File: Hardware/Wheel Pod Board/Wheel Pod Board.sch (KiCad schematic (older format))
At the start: 30 parts, among them J1 Conn_RJ-45, P1 UIM240XX_Stepper_Conn, P2 RS232, P3 ST_SWD_Connector, P4 SyRen, P5 BATT, U1 STM32F401RCT6, U2 SN75176BDR, U3 ZXCT1107, U4 ZXCT1107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

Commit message: Add ADC channels to cube, kicad something
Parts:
- P4: footprint MAVRIC_footprints:1x3_SMD_header -> Wire_Pads:SolderWirePad_3x_0-8mmDrill
- P5: footprint MAVRIC_footprints:1x2_SMD_header -> Wire_Pads:SolderWirePad_2x_0-8mmDrill
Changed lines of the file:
@@
 $EndComp
 $Comp
-L GND #PWR09
+L GND #PWR08
 U 1 1 54F82F5F
 P 7300 5750
-F 0 "#PWR09" H 7300 5500 60  0001 C CNN
+F 0 "#PWR08" H 7300 5500 60  0001 C CNN
 F 1 "GND" H 7300 5600 60  0000 C CNN
 F 2 "" H 7300 5750 60  0000 C CNN
@@
 $EndComp
 $Comp
-L GND #PWR010
+L GND #PWR09
 U 1 1 54F83FA9
 P 6550 5050
-F 0 "#PWR010" H 6550 4800 60  0001 C CNN
+F 0 "#PWR09" H 6550 4800 60  0001 C CNN
 F 1 "GND" H 6550 4900 60  0000 C CNN
 F 2 "" H 6550 5050 60  0000 C CNN
@@
 Connection ~ 7250 3900
 $Comp
-L +3V3 #PWR011
+L +3V3 #PWR010
 U 1 1 54F898ED
 P 4350 7400
-F 0 "#PWR011" H 4350 7250 60  0001 C CNN
+F 0 "#PWR010" H 4350 7250 60  0001 C CNN
 F 1 "+3V3" H 4350 7540 60  0000 C CNN
 F 2 "" H 4350 7400 60  0000 C CNN
@@
 	4350 7300 5000 7300
 $Comp
-L PWR_FLAG #FLG012
+L PWR_FLAG #FLG011
 U 1 1 54F89ADE
 P 4650 7350
-F 0 "#FLG012" H 4650 7445 30  0001 C CNN
+F 0 "#FLG011" H 4650 7445 30  0001 C CNN
 F 1 "PWR_FLAG" H 4650 7530 30  0000 C CNN
 F 2 "" H 4650 7350 60  0000 C CNN
@@
 $EndComp
 $Comp
-L +5V #PWR013
+L +5V #PWR012
 U 1 1 54F89B19
 P 4400 6800
-F 0 "#PWR013" H 4400 6650 60  0001 C CNN
+F 0 "#PWR012" H 4400 6650 60  0001 C CNN
 F 1 "+5V" H 4400 6940 60  0000 C CNN
 F 2 "" H 4400 6800 60  0000 C CNN
@@
 $EndComp
 $Comp
-L GND #PWR014
+L GND #PWR013
 U 1 1 54F91E0A
 P 10800 2450
-F 0 "#PWR014" H 10800 2200 60  0001 C CNN
+F 0 "#PWR013" H 10800 2200 60  0001 C CNN
 F 1 "GND" H 10800 2300 60  0000 C CNN
 F 2 "" H 10800 2450 60  0000 C CNN
@@
 F 0 "P5" H 6700 3700 50  0000 C CNN
 F 1 "BATT" H 6700 3400 50  0000 C CNN
-F 2 "MAVRIC_footprints:1x2_SMD_header" H 6700 3550 60  0001 C CNN
+F 2 "Wire_Pads:SolderWirePad_2x_0-8mmDrill" H 6700 3550 60  0001 C CNN
 F 3 "" H 6700 3550 60  0000 C CNN
 	1    6700 3550
@@
 $EndComp
 $Comp
-L GND #PWR015
+L GND #PWR014
 U 1 1 54F97284
 P 8450 5050
-F 0 "#PWR015" H 8450 4800 60  0001 C CNN
+F 0 "#PWR014" H 8450 4800 60  0001 C CNN
 F 1 "GND" H 8450 4900 60  0000 C CNN
 F 2 "" H 8450 5050 60  0000 C CNN
@@
 	10950 3500 10950 3800
 $Comp
-L GND #PWR016
+L GND #PWR015
 U 1 1 54F987F3
 P 10950 3800
-F 0 "#PWR016" H 10950 3550 60  0001 C CNN
+F 0 "#PWR015" H 10950 3550 60  0001 C CNN
 F 1 "GND" H 10950 3650 60  0000 C CNN
 F 2 "" H 10950 3800 60  0000 C CNN
@@
 Connection ~ 9150 3600
 $Comp
-L +12V #PWR017
+L +12V #PWR016
 U 1 1 54F9E120
 P 10700 3800
-F 0 "#PWR017" H 10700 3650 60  0001 C CNN
+F 0 "#PWR016" H 10700 3650 60  0001 C CNN
 F 1 "+12V" H 10700 3940 60  0000 C CNN
 F 2 "" H 10700 3800 60  0000 C CNN
@@
 $EndComp
 $Comp
-L PWR_FLAG #FLG018
+L PWR_FLAG #FLG017
 U 1 1 54F9E134
 P 7050 3600
-F 0 "#FLG018" H 7050 3695 30  0001 C CNN
+F 0 "#FLG017" H 7050 3695 30  0001 C CNN
 F 1 "PWR_FLAG" H 7050 3780 30  0000 C CNN
 F 2 "" H 7050 3600 60  0000 C CNN
@@
 $EndComp
 $Comp
-L PWR_FLAG #FLG019
+L PWR_FLAG #FLG018
 U 1 1 54F9E417
 P 7050 3500
-F 0 "#FLG019" H 7050 3595 30  0001 C CNN
+F 0 "#FLG018" H 7050 3595 30  0001 C CNN
 F 1 "PWR_FLAG" H 7050 3680 30  0000 C CNN
 F 2 "" H 7050 3500 60  0000 C CNN
@@
 Connection ~ 9750 3500
 $Comp
-L +3V3 #PWR020
+L +3V3 #PWR019
 U 1 1 54FA32A7
 P 7350 1500
-F 0 "#PWR020" H 7350 1350 60  0001 C CNN
+F 0 "#PWR019" H 7350 1350 60  0001 C CNN
 F 1 "+3V3" H 7350 1640 60  0000 C CNN
 F 2 "" H 7350 1500 60  0000 C CNN
@@
 $EndComp
 $Comp
-L +5V #PWR021
+L +5V #PWR020
 U 1 1 54FA4C38
 P 3450 6750
-F 0 "#PWR021" H 3450 6600 60  0001 C CNN
+F 0 "#PWR020" H 3450 6600 60  0001 C CNN
 F 1 "+5V" H 3450 6890 60  0000 C CNN
 F 2 "" H 3450 6750 60  0000 C CNN
@@
 Stp+12V
 $Comp
-L +5V #PWR022
+L +5V #PWR021
 U 1 1 54FACDEA
 P 7600 5850
-F 0 "#PWR022" H 7600 5700 60  0001 C CNN
+F 0 "#PWR021" H 7600 5700 60  0001 C CNN
 F 1 "+5V" H 7600 5990 60  0000 C CNN
 F 2 "" H 7600 5850 60  0000 C CNN
@@
 	10450 6050 10450 6100
 $Comp
-L GND #PWR023
+L GND #PWR022
 U 1 1 54FB0646
 P 10450 6100
-F 0 "#PWR023" H 10450 5850 60  0001 C CNN
+F 0 "#PWR022" H 10450 5850 60  0001 C CNN
 F 1 "GND" H 10450 5950 60  0000 C CNN
 F 2 "" H 10450 6100 60  0000 C CNN
@@
 	4400 6900 5000 6900
 $Comp
-L PWR_FLAG #FLG024
+L PWR_FLAG #FLG023
 U 1 1 54F9E182
 P 4650 6850
-F 0 "#FLG024" H 4650 6945 30  0001 C CNN
+F 0 "#FLG023" H 4650 6945 30  0001 C CNN
 F 1 "PWR_FLAG" H 4650 7030 30  0000 C CNN
 F 2 "" H 4650 6850 60  0000 C CNN
@@
 Connection ~ 4850 7400
 $Comp
-L GND #PWR025
+L GND #PWR024
 U 1 1 54F9E9CC
 P 4850 7500
-F 0 "#PWR025" H 4850 7250 60  0001 C CNN
+F 0 "#PWR024" H 4850 7250 60  0001 C CNN
 F 1 "GND" H 4850 7350 60  0000 C CNN
 F 2 "" H 4850 7500 60  0000 C CNN
@@
 F 0 "P4" H 10150 4050 50  0000 C CNN
 F 1 "SyRen" H 10150 3650 50  0000 C CNN
-F 2 "MAVRIC_footprints:1x3_SMD_header" H 10150 3850 60  0001 C CNN
+F 2 "Wire_Pads:SolderWirePad_3x_0-8mmDrill" H 10150 3850 60  0001 C CNN
 F 3 "" H 10150 3850 60  0000 C CNN
 	1    10150 3850

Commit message: Progress on new pcb route
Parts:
- P3: footprint MAVRIC_footprints:1x6_SMD_header -> MAVRIC_footprints:SolderWirePad_6xInline_0-8mmDrill
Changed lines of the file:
@@
 F 0 "P3" H 9200 6300 50  0000 C CNN
 F 1 "ST_SWD_Connector" H 9200 5600 50  0000 C CNN
-F 2 "MAVRIC_footprints:1x6_SMD_header" H 9200 5950 60  0001 C CNN
+F 2 "MAVRIC_footprints:SolderWirePad_6xInline_0-8mmDrill" H 9200 5950 60  0001 C CNN
 F 3 "" H 9200 5950 60  0000 C CNN
 	1    9200 5950

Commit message: Attach 485 TX enable to micro
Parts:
- P3: footprint MAVRIC_footprints:SolderWirePad_6xInline_0-8mmDrill -> MAVRIC_footprints:1x6_SMD_header
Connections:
- net TX_EN: now reaches U1.50 (PA15)
- net TX_EN: now also U2.2 (~RE), U2.3 (DE)
- no-connect marks 41 -> 40
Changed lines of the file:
@@
 F 0 "P3" H 9200 6300 50  0000 C CNN
 F 1 "ST_SWD_Connector" H 9200 5600 50  0000 C CNN
-F 2 "MAVRIC_footprints:SolderWirePad_6xInline_0-8mmDrill" H 9200 5950 60  0001 C CNN
+F 2 "MAVRIC_footprints:1x6_SMD_header" H 9200 5950 60  0001 C CNN
 F 3 "" H 9200 5950 60  0000 C CNN
 	1    9200 5950
@@
 NoConn ~ 1650 2250
 NoConn ~ 1650 2350
-NoConn ~ 1650 2650
 NoConn ~ 1650 3000
 NoConn ~ 1650 3100
@@
 Text Label 7600 5650 2    60   ~ 0
 Stp+12V
+Wire Wire Line
+	1650 2650 1800 2650
+Text Label 1800 2650 0    60   ~ 0
+TX_EN
+Text Label 1750 7000 2    60   ~ 0
+TX_EN
 $EndSCHEMATC

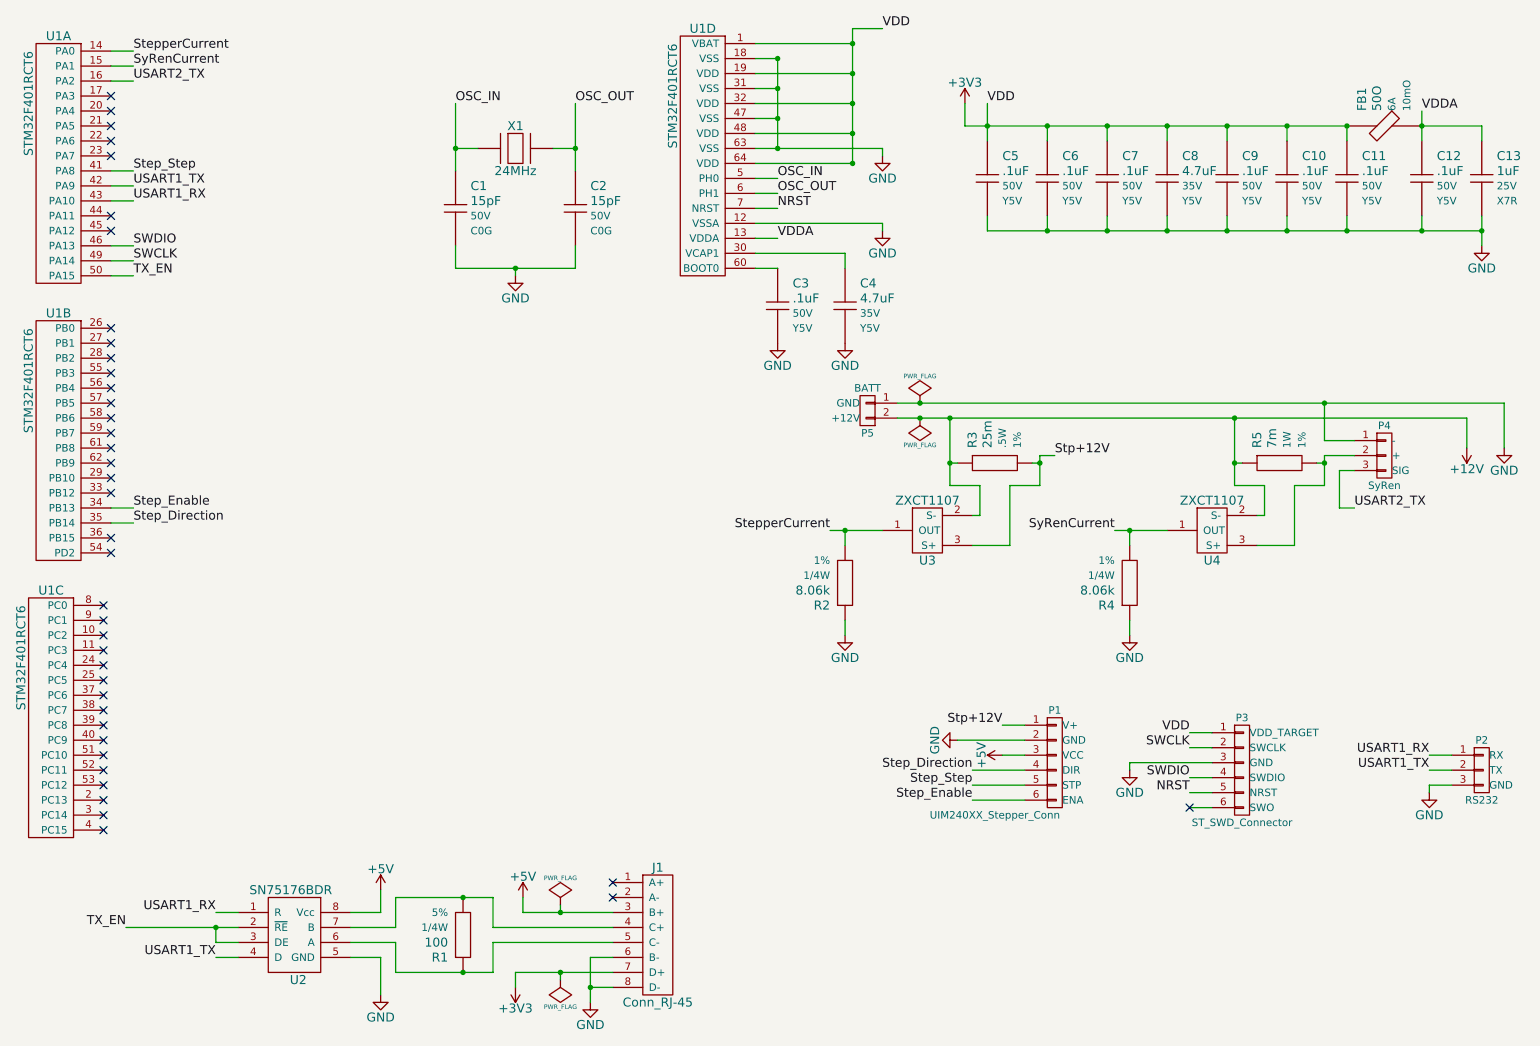
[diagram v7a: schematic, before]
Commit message: Add red and green LEDs to board
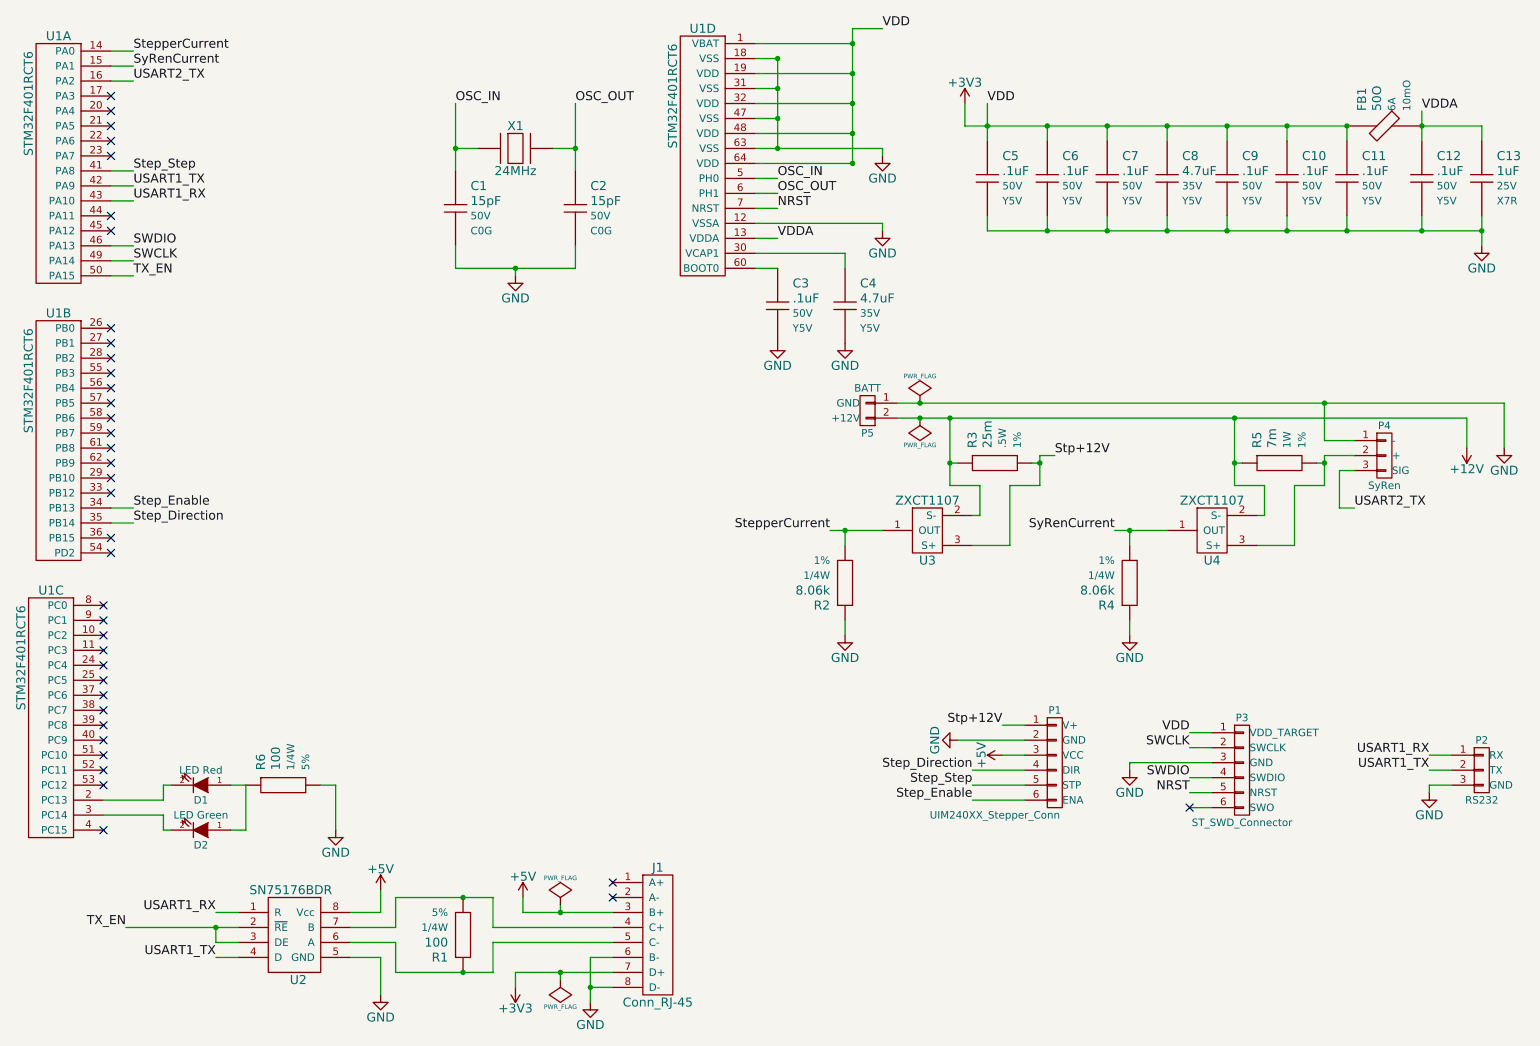
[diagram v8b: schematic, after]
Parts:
- added D1: LED Red, Resistors_SMD:R_0805_HandSoldering, symbol LED
- added D2: LED Green, Resistors_SMD:R_0805_HandSoldering, symbol LED
- added R6: 100, Resistors_SMD:R_1206_HandSoldering, symbol Resistor
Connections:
- net GND: now also R6.2
- net at U1.2 (PC13): now also D1.2 (K)
- net at U1.3 (PC14): now also D2.2 (K)
- new net: D1.1 (A), D2.1 (A), R6.1
- no-connect marks 40 -> 38
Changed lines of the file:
@@
 LIBS:MAVRIClib
 LIBS:Connectors
+LIBS:Actives
 LIBS:Wheel Pod Board-cache
 EELAYER 25 0
@@
 Connection ~ 6100 1400
 Wire Wire Line
-	5950 1800 6800 1800
+	5950 1800 6100 1800
+Wire Wire Line
+	6100 1800 6800 1800
 Connection ~ 6100 1800
 Wire Wire Line
@@
 Connection ~ 6600 1100
 Wire Wire Line
-	6100 1200 6100 1800
-Wire Wire Line
-	6600 1000 6600 1900
+	6100 1200 6100 1400
+Wire Wire Line
+	6100 1400 6100 1600
+Wire Wire Line
+	6100 1600 6100 1800
+Wire Wire Line
+	6600 1000 6600 1100
+Wire Wire Line
+	6600 1100 6600 1300
+Wire Wire Line
+	6600 1300 6600 1500
+Wire Wire Line
+	6600 1500 6600 1700
+Wire Wire Line
+	6600 1700 6600 1900
 Wire Wire Line
 	5950 2600 6100 2600
@@
 	2350 7100 2500 7100
 Wire Wire Line
-	1750 7000 2500 7000
+	1750 7000 2350 7000
+Wire Wire Line
+	2350 7000 2500 7000
 Wire Wire Line
 	2500 7200 2350 7200
@@
 	9900 1650 9900 1750
 Wire Wire Line
-	7500 1500 7500 1750
+	7500 1500 7500 1650
+Wire Wire Line
+	7500 1650 7500 1750
 Connection ~ 7500 1650
 Wire Wire Line
@@
 Connection ~ 9900 2350
 Wire Wire Line
-	10400 1550 10400 1750
+	10400 1550 10400 1650
+Wire Wire Line
+	10400 1650 10400 1750
 Connection ~ 9900 1650
 Connection ~ 10400 1650
@@
 	10800 1650 10800 1750
 Wire Wire Line
-	10800 2250 10800 2450
+	10800 2250 10800 2350
+Wire Wire Line
+	10800 2350 10800 2450
 Wire Wire Line
 	10400 2350 10400 2250
@@
 	10400 1650 10800 1650
 Wire Wire Line
-	7500 2350 10800 2350
-Wire Wire Line
-	7350 1650 9900 1650
+	7500 2350 7900 2350
+Wire Wire Line
+	7900 2350 8300 2350
+Wire Wire Line
+	8300 2350 8700 2350
+Wire Wire Line
+	8700 2350 9100 2350
+Wire Wire Line
+	9100 2350 9500 2350
+Wire Wire Line
+	9500 2350 9900 2350
+Wire Wire Line
+	9900 2350 10400 2350
+Wire Wire Line
+	10400 2350 10800 2350
+Wire Wire Line
+	7350 1650 7500 1650
+Wire Wire Line
+	7500 1650 7900 1650
+Wire Wire Line
+	7900 1650 8300 1650
+Wire Wire Line
+	8300 1650 8700 1650
+Wire Wire Line
+	8700 1650 9100 1650
+Wire Wire Line
+	9100 1650 9500 1650
+Wire Wire Line
+	9500 1650 9900 1650
 Wire Wire Line
 	7350 1500 7350 1650
@@
 OSC_OUT
 Wire Wire Line
-	3950 1500 3950 1950
+	3950 1500 3950 1800
+Wire Wire Line
+	3950 1800 3950 1950
 Wire Wire Line
 	3950 1800 4100 1800
@@
 	4600 1800 4750 1800
 Wire Wire Line
-	4750 1500 4750 1950
+	4750 1500 4750 1800
+Wire Wire Line
+	4750 1800 4750 1950
 Wire Wire Line
 	3950 2450 3950 2600
 Wire Wire Line
-	3950 2600 4750 2600
+	3950 2600 4350 2600
+Wire Wire Line
+	4350 2600 4750 2600
 Wire Wire Line
 	4750 2600 4750 2450
@@
 	7450 4050 7450 4250
 Wire Wire Line
-	6450 4350 6800 4350
+	6450 4350 6550 4350
+Wire Wire Line
+	6550 4350 6800 4350
 Wire Wire Line
 	6550 4450 6550 4350
@@
 	7850 3900 7800 3900
 Wire Wire Line
-	7250 3600 7250 4050
+	7250 3600 7250 3900
+Wire Wire Line
+	7250 3900 7250 4050
 Wire Wire Line
 	7300 3900 7250 3900
@@
 $EndComp
 Wire Wire Line
-	4350 7300 5000 7300
+	4350 7300 4650 7300
+Wire Wire Line
+	4650 7300 5000 7300
 $Comp
 L PWR_FLAG #FLG011
@@
 $EndComp
 Wire Wire Line
-	7850 3850 7850 4050
+	7850 3850 7850 3900
+Wire Wire Line
+	7850 3900 7850 4050
 Wire Wire Line
 	6550 4950 6550 5050
@@
 StepperCurrent
 Wire Wire Line
-	6900 3600 10700 3600
+	6900 3600 7050 3600
+Wire Wire Line
+	7050 3600 7250 3600
+Wire Wire Line
+	7250 3600 9150 3600
+Wire Wire Line
+	9150 3600 10700 3600
 $Comp
 L ZXCT1107 U4
@@
 	9350 4050 9350 4250
 Wire Wire Line
-	8350 4350 8700 4350
+	8350 4350 8450 4350
+Wire Wire Line
+	8450 4350 8700 4350
 Wire Wire Line
 	8450 4450 8450 4350
@@
 	9750 3900 9700 3900
 Wire Wire Line
-	9150 3600 9150 4050
+	9150 3600 9150 3900
+Wire Wire Line
+	9150 3900 9150 4050
 Wire Wire Line
 	9200 3900 9150 3900
@@
 SyRenCurrent
 Wire Wire Line
-	6900 3500 10950 3500
+	6900 3500 7050 3500
+Wire Wire Line
+	7050 3500 9750 3500
+Wire Wire Line
+	9750 3500 10950 3500
 Wire Wire Line
 	10950 3500 10950 3800
@@
 Connection ~ 7250 3600
 Wire Wire Line
-	9750 3850 9750 4050
+	9750 3850 9750 3900
+Wire Wire Line
+	9750 3900 9750 4050
 Wire Wire Line
 	9750 3850 9950 3850
@@
 	3550 7000 3550 6800
 Wire Wire Line
-	3550 6800 4200 6800
+	3550 6800 4000 6800
+Wire Wire Line
+	4000 6800 4200 6800
 Wire Wire Line
 	4200 6800 4200 7000
@@
 	3550 7100 3550 7300
 Wire Wire Line
-	3550 7300 4200 7300
+	3550 7300 4000 7300
+Wire Wire Line
+	4000 7300 4200 7300
 Wire Wire Line
 	4200 7300 4200 7100
@@
 Connection ~ 4650 7300
 Wire Wire Line
-	4400 6900 5000 6900
+	4400 6900 4650 6900
+Wire Wire Line
+	4650 6900 5000 6900
 $Comp
 L PWR_FLAG #FLG023
@@
 	5000 7200 4850 7200
 Wire Wire Line
-	4850 7200 4850 7500
+	4850 7200 4850 7400
+Wire Wire Line
+	4850 7400 4850 7500
 Wire Wire Line
 	5000 7400 4850 7400
@@
 NoConn ~ 1650 3400
 NoConn ~ 1650 3500
-NoConn ~ 1650 3600
-NoConn ~ 1650 3700
 NoConn ~ 1650 3800
 NoConn ~ 1650 3900
@@
 NoConn ~ 1600 5950
 NoConn ~ 1600 6050
-NoConn ~ 1600 6150
-NoConn ~ 1600 6250
 NoConn ~ 1600 6350
 NoConn ~ 5000 6700
@@
 Text Label 1750 7000 2    60   ~ 0
 TX_EN
+$Comp
+L LED D1
+U 1 1 54FBC1C4
+P 2250 6050
+F 0 "D1" H 2250 6150 50  0000 C CNN
+F 1 "LED Red" H 2250 5950 50  0000 C CNN
+F 2 "Resistors_SMD:R_0805_HandSoldering" H 2250 6050 60  0001 C CNN
+F 3 "" H 2250 6050 60  0000 C CNN
+F 4 "Digi-Key" H 2250 6050 60  0001 C CNN "Vendor"
+F 5 "475-1415-1-ND" H 2250 6050 60  0001 C CNN "Vendor Part #"
+	1    2250 6050
+	-1   0    0    1
+$EndComp
+$Comp
+L Resistor R6
+U 1 1 54FBC795
+P 2800 6050
+F 0 "R6" V 2650 6150 60  0000 L CNN
+F 1 "100" V 2750 6150 60  0000 L CNN
+F 2 "Resistors_SMD:R_1206_HandSoldering" H 2700 6050 60  0001 C CNN
+F 3 "" H 2800 6150 60  0001 C CNN
+F 4 "Panasonic" H 2800 6050 60  0001 C CNN "Manufacturer"
+F 5 "ERJ-8GEYJ101V" H 2800 6050 60  0001 C CNN "Manufacturer Part #"
+F 6 "Digi-Key" H 2800 6050 60  0001 C CNN "Vendor"
+F 7 "P100ECT-ND" H 2800 6050 60  0001 C CNN "Vendor Part #"
+F 8 "1/4W" V 2850 6150 50  0000 L CNN "Power"
+F 9 "5%" V 2950 6150 50  0000 L CNN "Tolerance"
+	1    2800 6050
+	1    0    0    -1
+$EndComp
+Wire Wire Line
+	2000 6150 1600 6150
+Wire Wire Line
+	2000 6150 2000 6050
+Wire Wire Line
+	2000 6050 2050 6050
+Wire Wire Line
+	1600 6250 2000 6250
+Wire Wire Line
+	2000 6250 2000 6350
+$Comp
+L LED D2
+U 1 1 54FBDF6F
+P 2250 6350
+F 0 "D2" H 2250 6450 50  0000 C CNN
+F 1 "LED Green" H 2250 6250 50  0000 C CNN
+F 2 "Resistors_SMD:R_0805_HandSoldering" H 2250 6350 60  0001 C CNN
+F 3 "" H 2250 6350 60  0000 C CNN
+F 4 "Digi-Key" H 2250 6350 60  0001 C CNN "Vendor"
+F 5 "475-1410-1-ND" H 2250 6350 60  0001 C CNN "Vendor Part #"
+	1    2250 6350
+	-1   0    0    1
+$EndComp
+Wire Wire Line
+	2000 6350 2050 6350
+Wire Wire Line
+	3150 6050 3150 6350
+$Comp
+L GND #PWR025
+U 1 1 54FBE69D
+P 3150 6350
+F 0 "#PWR025" H 3150 6100 60  0001 C CNN
+F 1 "GND" H 3150 6200 60  0000 C CNN
+F 2 "" H 3150 6350 60  0000 C CNN
+F 3 "" H 3150 6350 60  0000 C CNN
+	1    3150 6350
+	1    0    0    -1
+$EndComp
+NoConn ~ 1650 3700
+NoConn ~ 1650 3600
+Wire Wire Line
+	2450 6350 2550 6350
+Wire Wire Line
+	2550 6350 2550 6050
+Wire Wire Line
+	2550 6050 2450 6050
+Wire Wire Line
+	3050 6050 3150 6050
 $EndSCHEMATC
